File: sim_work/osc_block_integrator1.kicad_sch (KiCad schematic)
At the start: 6 parts, among them U1 ADA4530-1

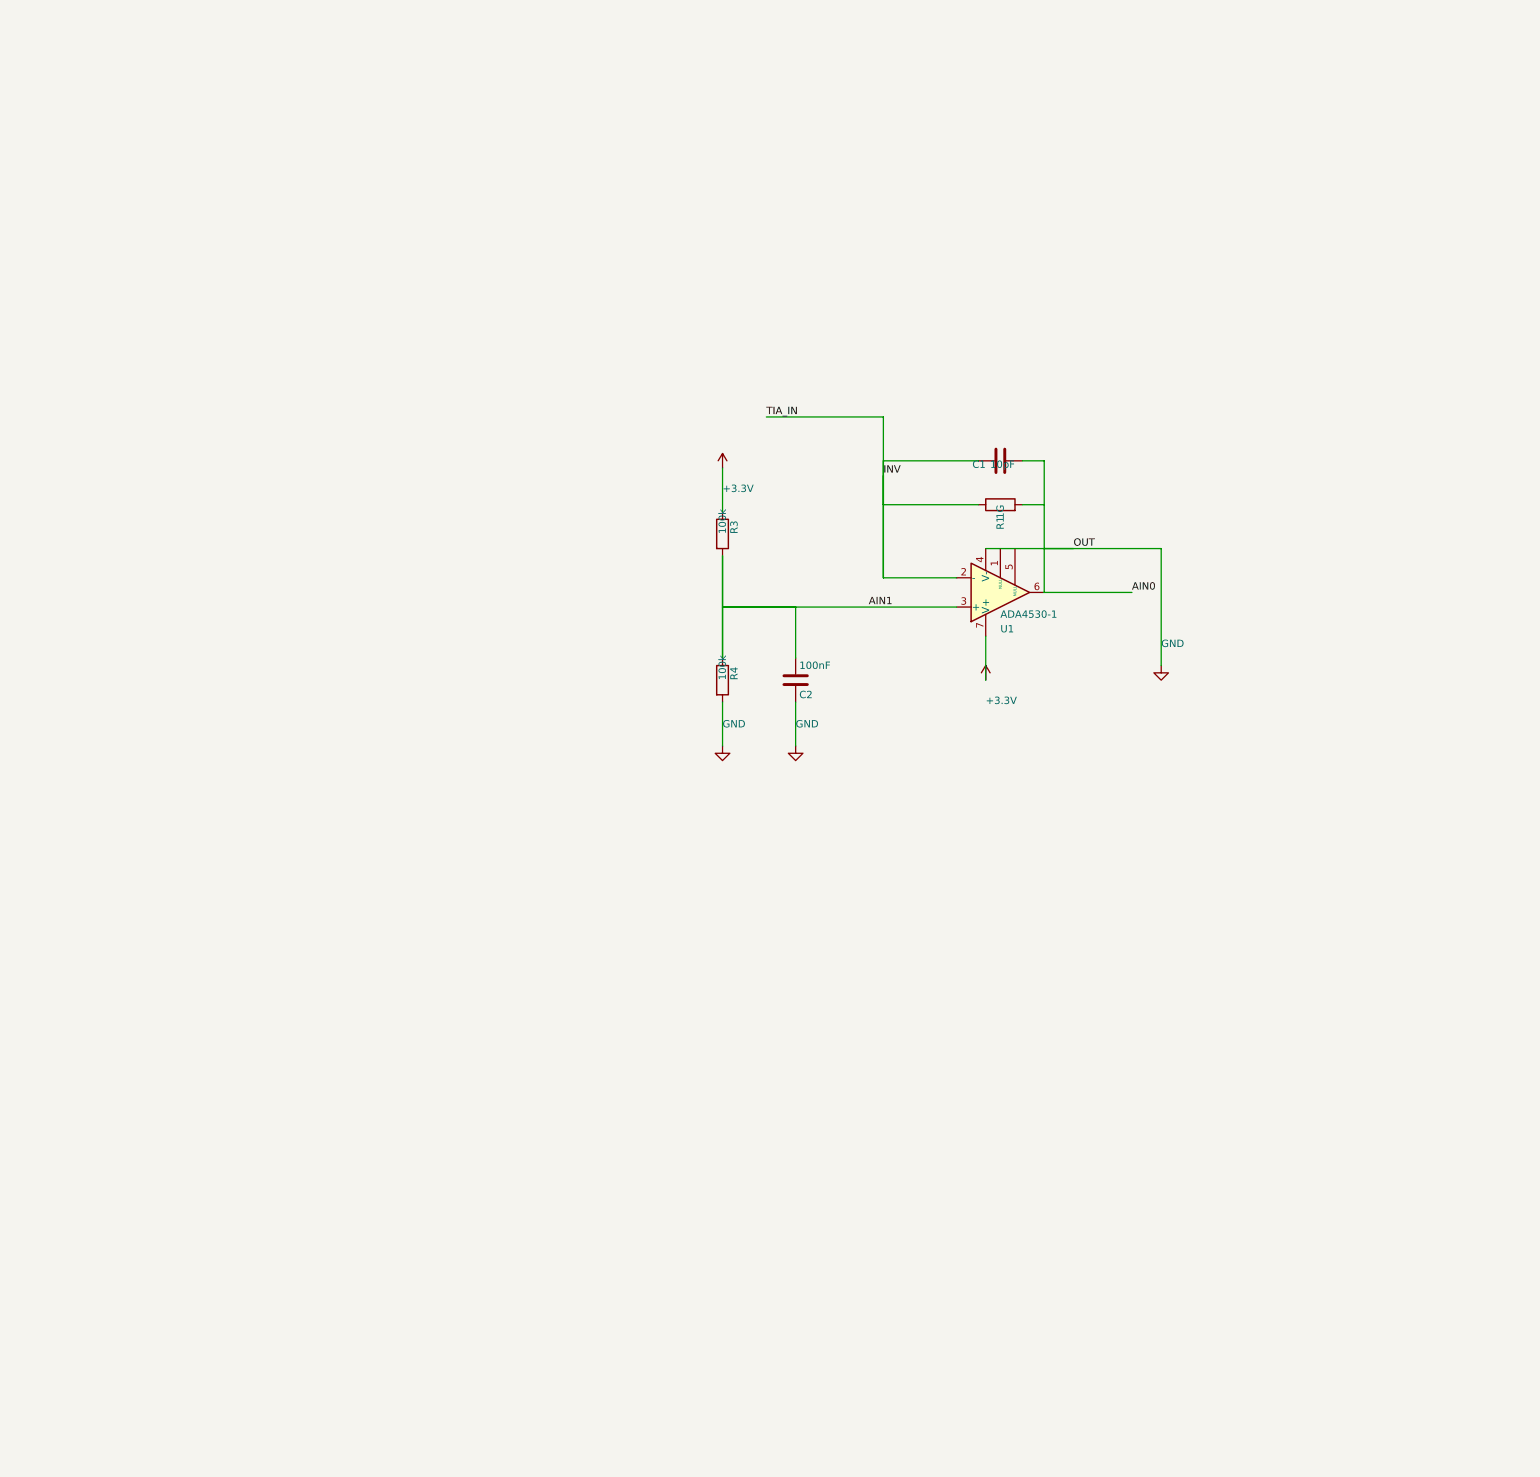
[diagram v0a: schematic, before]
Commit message: Per-block PDF schematics: 6 oscillator + 6 TIA blocks with merged PDFs
Add individual A4 schematic generation for each functional circuit block:
- Oscillator: summing amp, integrator 1/2, RMS detector, power supply, MCU
- TIA: input filters, analog mux, mux TIA, relay ladder, MCU section, electrometer
- merge_pdfs() helper using PyMuPDF for multi-page output
- CLI commands: osc_blocks, tia_blocks
- All blocks verified: 0 wire crossings, complete pin connectivity

Co-Authored-By: Claude Opus 4.6 <noreply@anthropic.com>
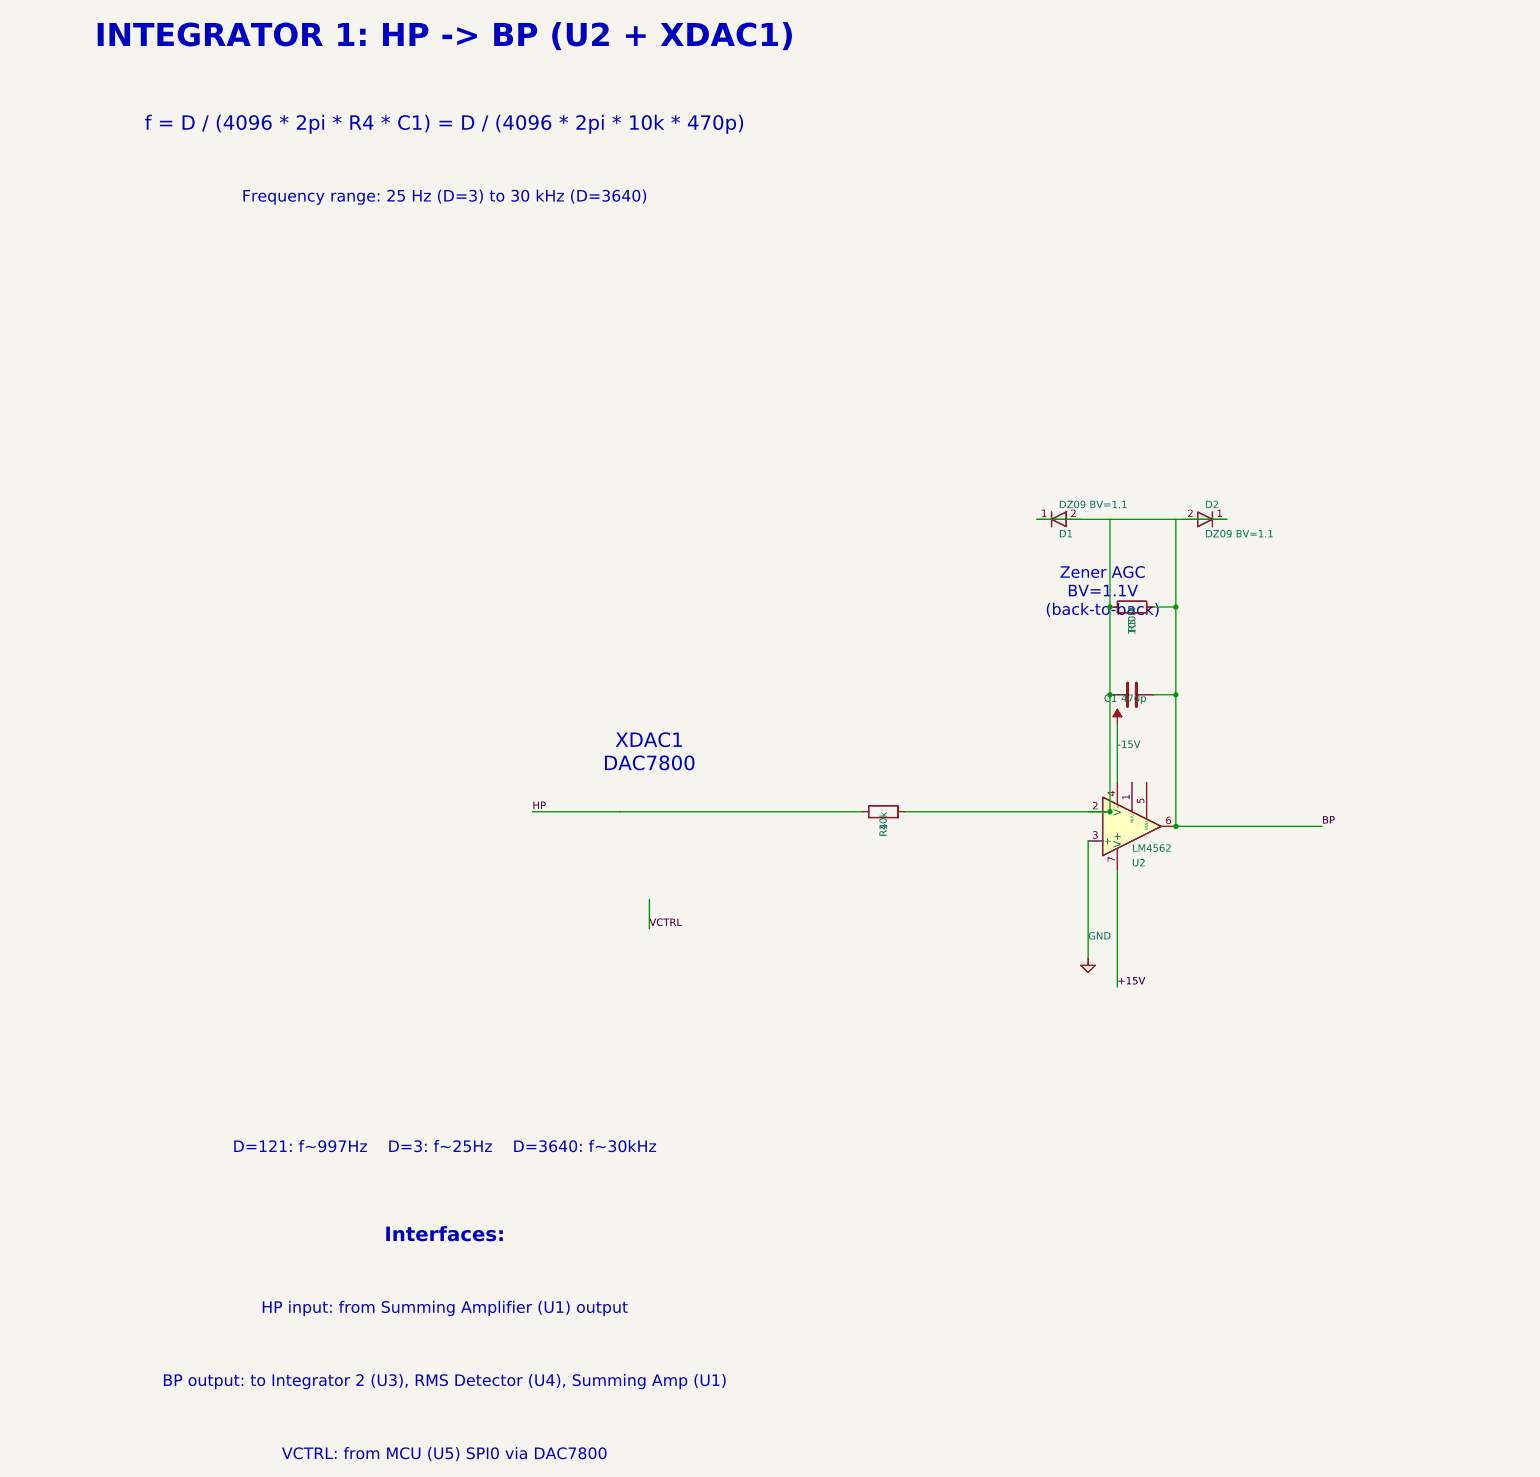
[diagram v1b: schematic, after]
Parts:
- removed C2: 100nF, symbol C:C
- removed R1: 1G, symbol R:R
- removed R3: 100k, symbol R:R
- removed U1: ADA4530-1, symbol LM741:LM741
- added D1, D2: DZ09 BV=1.1, symbol D:D
- added R5: 100M, symbol R:R
- added U2: LM4562, symbol LM741:LM741
- C1: value 10pF -> 470p
- R4: value 100k -> 10k
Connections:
- net GND: now also U2.3 (+); no longer R4.2
- net AIN0 renamed BP
- net BP: now also R5.2, U2.6
- net AIN1 renamed HP
- net INV: no longer names the net of C1.1
- net INV: now also R4.2, R5.1
- new net: D1.1 (K), D2.1 (K)
- new net +15V: U2.7 (V+)
- new net -15V: U2.4 (V-)
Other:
- note added: "BP output: to Integrator 2 (U3), RMS Detector (U4), Summing Amp (U1)"
- note added: "D=121: f~997Hz D=3: f~25Hz D=3640: f~30kHz"
- note added: "Frequency range: 25 Hz (D=3) to 30 kHz (D=3640)"
- note added: "HP input: from Summing Amplifier (U1) output"
- note added: "INTEGRATOR 1: HP -> BP (U2 + XDAC1)"
- note added: "Interfaces:"
- note added: "VCTRL: from MCU (U5) SPI0 via DAC7800"
- note added: "XDAC1 DAC7800"
- note added: "Zener AGC BV=1.1V (back-to-back)"
- note added: "f = D / (4096 * 2pi * R4 * C1) = D / (4096 * 2pi * 10k * 470p)"
- company: (none) -> CircuitForge
- title: TIA with Mux Interface - ADA4530-1 -> State Variable Oscillator - Integrator 1 (HP to BP)
